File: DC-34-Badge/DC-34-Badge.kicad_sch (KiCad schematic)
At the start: 17 parts, among them U1 ESP32-S3-MINI-1, U2 AP2112K-3.3

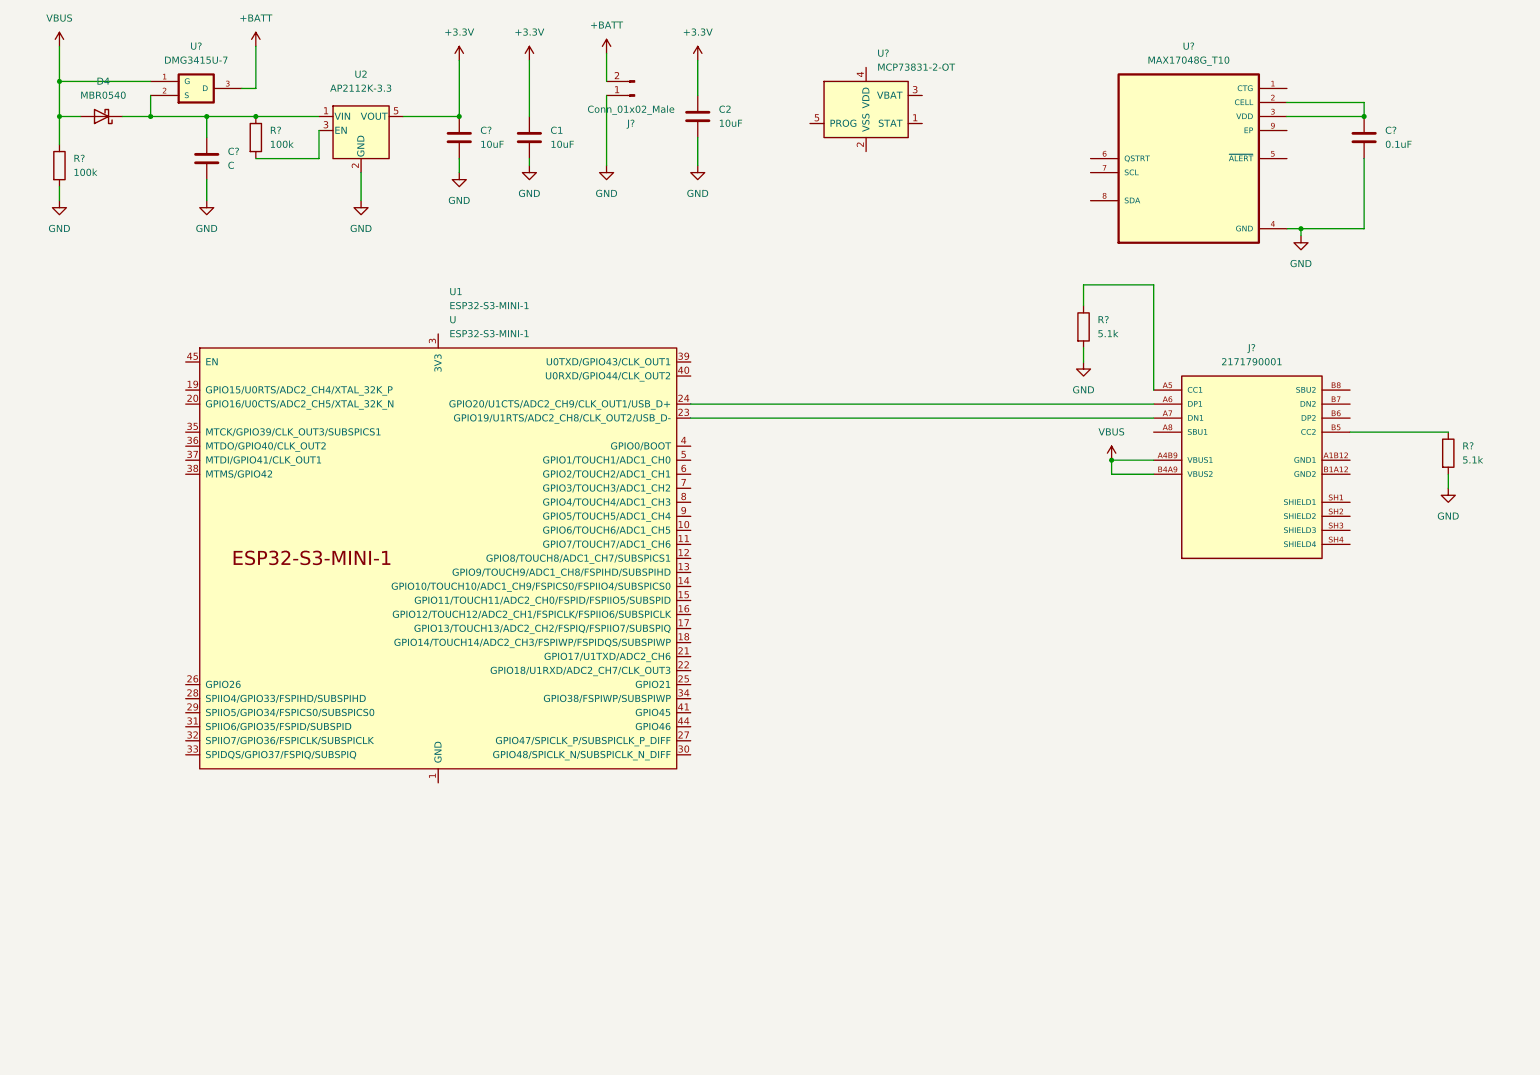
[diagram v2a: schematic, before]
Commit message: Completed Power System
Board design will power up.
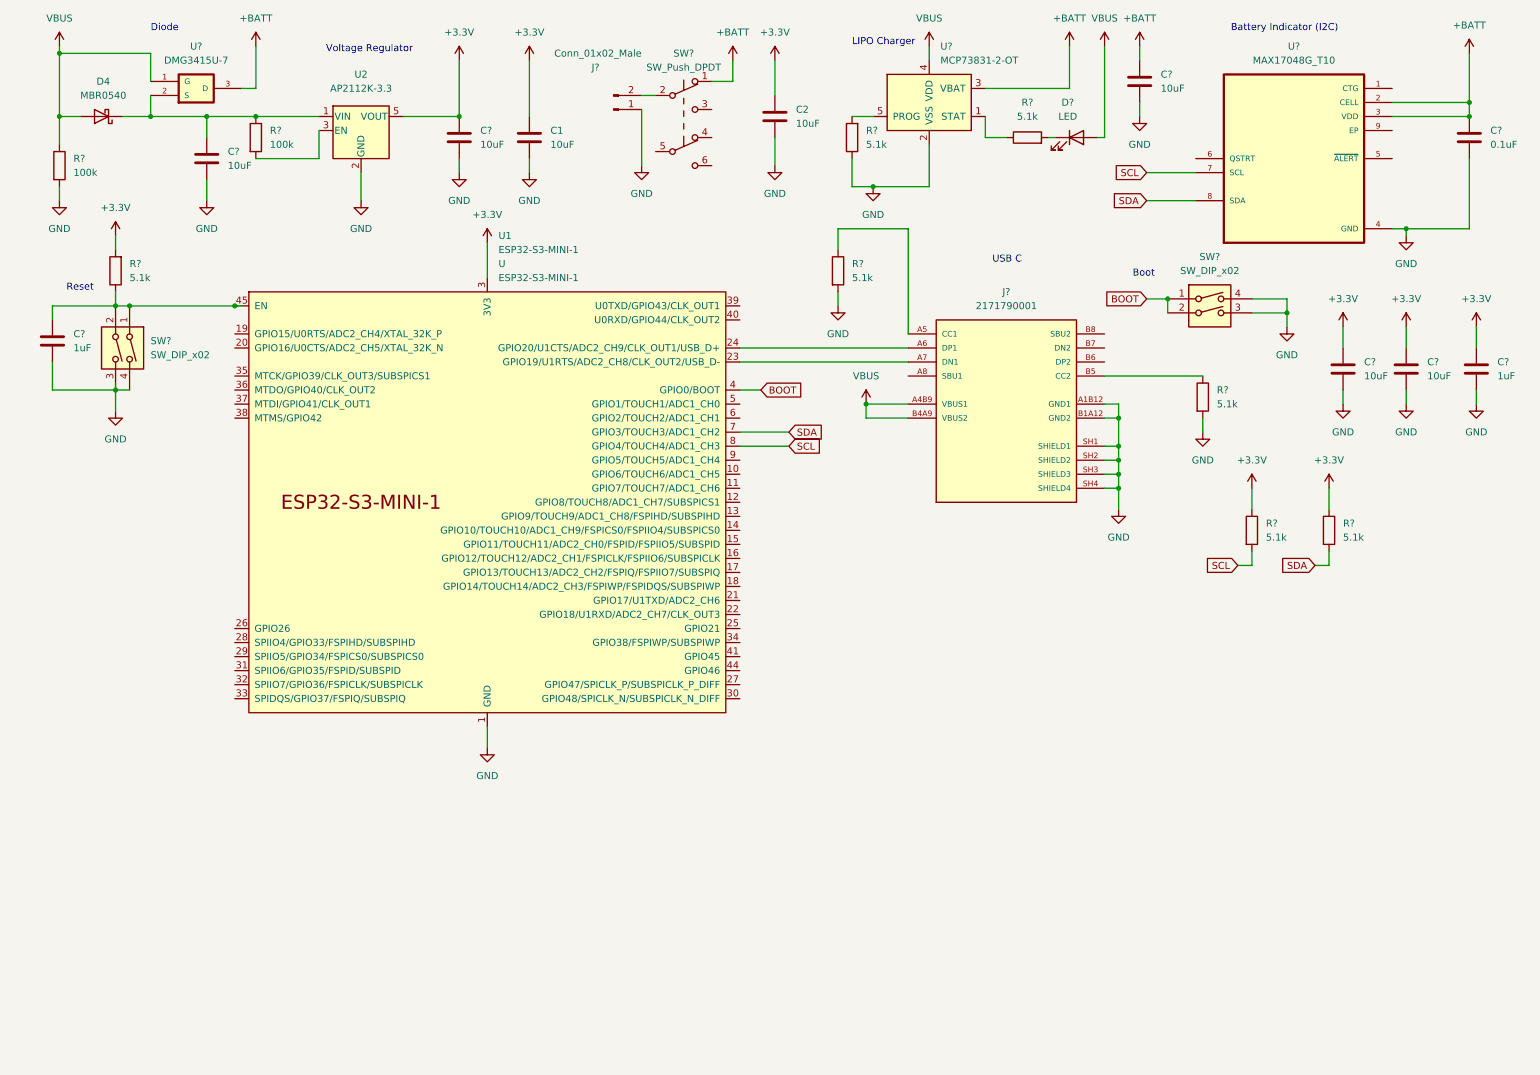
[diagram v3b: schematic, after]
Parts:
- added C? (x2): 1uF, Capacitor_SMD:C_0402_1005Metric, symbol Device:C
- added C? (x3): 10uF, Capacitor_SMD:C_0402_1005Metric, symbol Device:C
- added D?: LED, LED_SMD:LED_0201_0603Metric, symbol Device:LED
- added R? (x5): 5.1k, Resistor_SMD:R_0402_1005Metric, symbol Device:R
- added SW? (x2): SW_DIP_x02, Button_Switch_THT:SW_PUSH_6mm, symbol Switch:SW_DIP_x02
- added SW?: SW_Push_DPDT, Button_Switch_THT:SW_CuK_JS202011CQN_DPDT_Straight, symbol Switch:SW_Push_DPDT
- C?: value C -> 10uF
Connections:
- net +3.3V: now also U1.3 (3V3), C?.1, C?.1, C?.1, R?.1, R?.1, R?.2
- net +BATT: now also C?.1, U?.2 (CELL), U?.3 (VBAT), U?.3 (VDD), C?.1, SW?.1 (A); no longer J?.2 (Pin_2)
- net GND: now also J?.A1B12 (GND1), J?.B1A12 (GND2), J?.SH1 (SHIELD1), J?.SH2 (SHIELD2), J?.SH3 (SHIELD3), J?.SH4 (SHIELD4), U1.1 (GND), U1.2 (GND), U1.42 (GND), U1.43 (GND), U1.46 (GND), U1.47 (GND), U1.48 (GND), U1.49 (GND), U1.50 (GND), U1.51 (GND), U1.52 (GND), U1.53 (GND), U1.54 (GND), U1.55 (GND), U1.56 (GND), U1.57 (GND), U1.58 (GND), U1.59 (GND), U1.60 (GND), U1.61 (GND), U1.62 (GND), U1.63 (GND), U1.64 (GND), U1.65 (GND), U?.2 (VSS), C?.2, C?.2, C?.2, C?.2, C?.2, R?.1, SW?.3, SW?.3, SW?.4, SW?.4
- net VBUS: now also U?.4 (VDD), D?.2 (A)
- net BOOT: now reaches U1.4 (GPIO0/BOOT)
- net BOOT: now also SW?.1, SW?.2
- net at U1.45 (EN): now also C?.1, R?.1, SW?.1, SW?.2
- net SDA: now reaches U1.7 (GPIO3/TOUCH3/ADC1_CH2)
- net SDA: now also U?.8 (SDA), R?.2
- net SCL: now reaches U1.8 (GPIO4/TOUCH4/ADC1_CH3)
- net SCL: now also U?.7 (SCL), R?.2
- net at U?.1 (STAT): now also R?.1
- net at U?.5 (PROG): now also R?.2
- new net: D?.1 (K), R?.2
- new net: J?.2 (Pin_2), SW?.2 (B)
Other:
- note added: "Battery Indicator (I2C)"
- note added: "Boot"
- note added: "Diode"
- note added: "LIPO Charger"
- note added: "Reset"
- note added: "USB C"
- note added: "Voltage Regulator"
- moved on the sheet: C2, C?, J?, R?, U1, U?

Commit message: Base Design Complete
Full duplication of adafruit design.
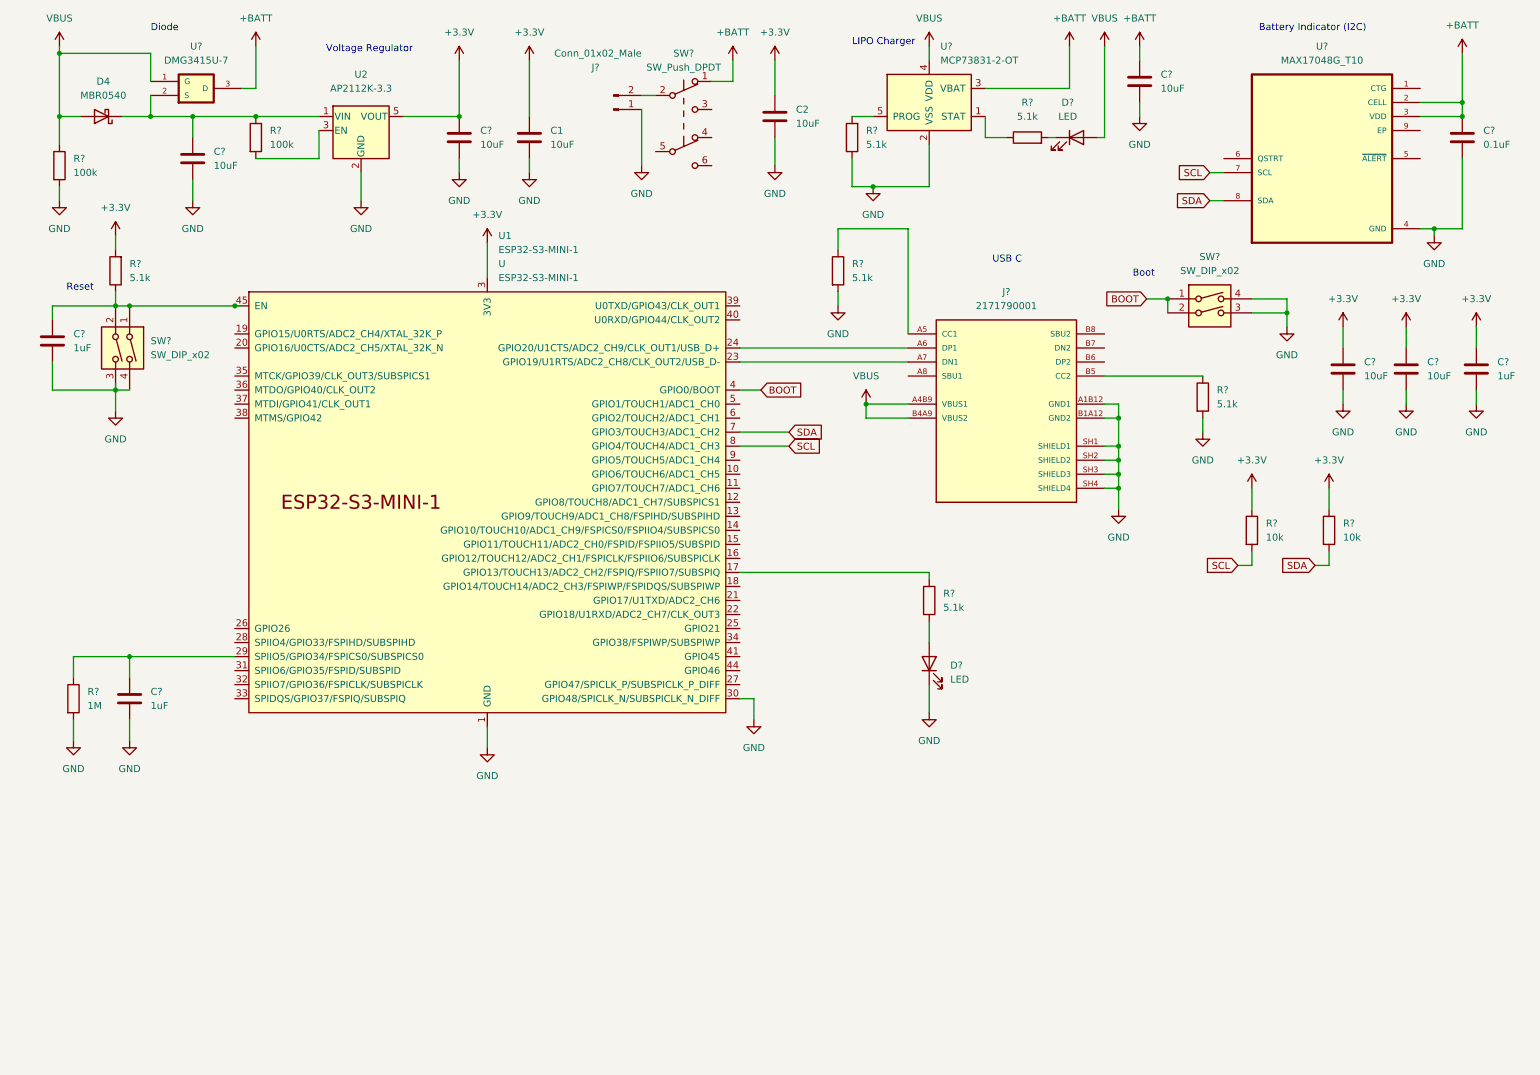
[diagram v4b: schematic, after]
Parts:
- added C?: 1uF, Capacitor_SMD:C_0402_1005Metric, symbol Device:C
- added D?: LED, LED_SMD:LED_0201_0603Metric, symbol Device:LED
- added R?: 1M, Resistor_SMD:R_0402_1005Metric, symbol Device:R
- added R?: 5.1k, Resistor_SMD:R_0402_1005Metric, symbol Device:R
- R? (x2): value 5.1k -> 10k
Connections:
- net GND: now also U1.30 (GPIO48/SPICLK_N/SUBSPICLK_N_DIFF), C?.2, D?.1 (K), R?.2
- net at U1.17 (GPIO13/TOUCH13/ADC2_CH2/FSPIQ/FSPIIO7/SUBSPIQ): now also R?.1
- net at U1.29 (SPIIO5/GPIO34/FSPICS0/SUBSPICS0): now also C?.1, R?.1
- new net: D?.2 (A), R?.2
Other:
- moved on the sheet: C?, U?

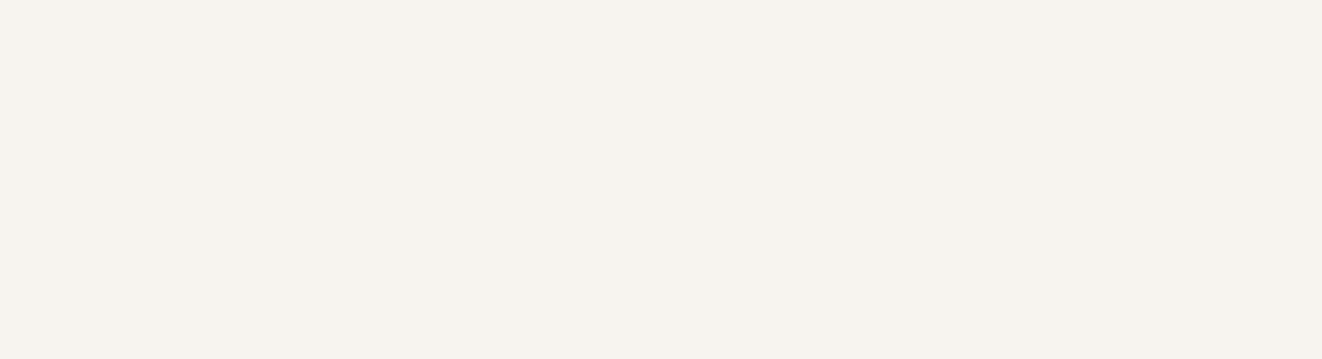
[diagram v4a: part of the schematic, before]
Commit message: Added ZIF Connector
Added ZIF connector symbol and footprint.
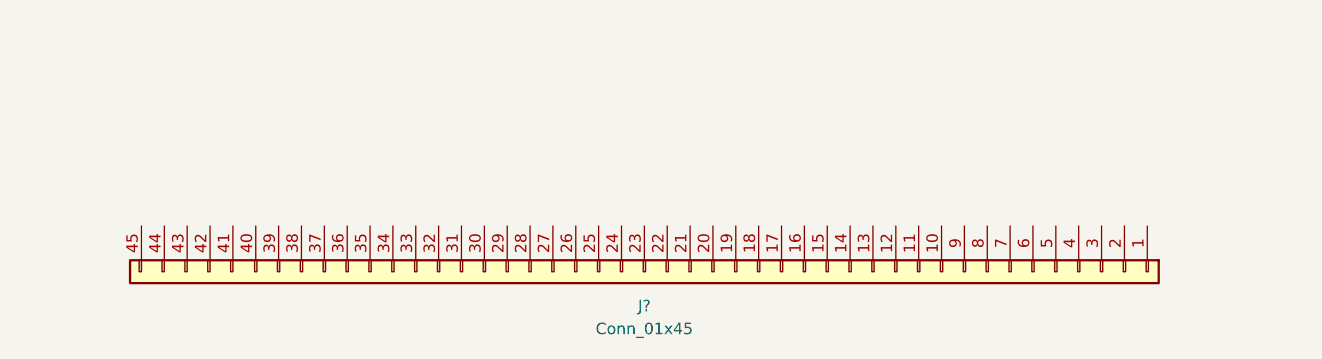
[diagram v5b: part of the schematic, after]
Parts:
- added J?: Conn_01x45, CF4245FH0R0:ZIF_45_0.5mm, symbol ZIF:Conn_01x45
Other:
- company: (none) -> Cyber Professionals Enthusiast Club
- title: (none) -> CPEC DEFCON 34 Badge
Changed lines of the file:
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@@
 (kicad_sch (version 20211123) (generator eeschema)
   (paper "A4")
+  (title_block
+    (title "CPEC DEFCON 34 Badge")
+    (date "3/27/2026")
+    (rev "0.1")
+    (company "Cyber Professionals Enthusiast Club")
+  )
   (junction (at 30.48 66.04) (diameter 0) (color 0 0 0 0)
   )
@@
     )
     (pin "1")
+  )
+  (symbol (lib_id "ZIF:Conn_01x45") (at 93.98 182.88 270) (unit 1)
+    (in_bom yes) (on_board yes) (fields_autoplaced)
+    (property "Reference" "J?" (id 0) (at 86.36 186.69 90))
+    (property "Value" "Conn_01x45" (id 1) (at 86.36 189.23 90))
+    (property "Footprint" "CF4245FH0R0:ZIF_45_0.5mm" (id 2) (at 93.98 182.88 0)
+      (effects (font (size 1.27 1.27)) hide)
+    )
+    (property "Datasheet" "~" (id 3) (at 93.98 182.88 0)
+      (effects (font (size 1.27 1.27)) hide)
+    )
+    (pin "1")
+    (pin "10")
+    (pin "11")
+    (pin "12")
+    (pin "13")
+    (pin "14")
+    (pin "15")
+    (pin "16")
+    (pin "17")
+    (pin "18")
+    (pin "19")
+    (pin "2")
+    (pin "20")
+    (pin "21")
+    (pin "22")
+    (pin "23")
+    (pin "24")
+    (pin "25")
+    (pin "26")
+    (pin "27")
+    (pin "28")
+    (pin "29")
+    (pin "3")
+    (pin "30")
+    (pin "31")
+    (pin "32")
+    (pin "33")
+    (pin "34")
+    (pin "35")
+    (pin "36")
+    (pin "37")
+    (pin "38")
+    (pin "39")
+    (pin "4")
+    (pin "40")
+    (pin "41")
+    (pin "42")
+    (pin "43")
+    (pin "44")
+    (pin "45")
+    (pin "5")
+    (pin "6")
+    (pin "7")
+    (pin "8")
+    (pin "9")
   )
   (symbol (lib_id "power:+3.3V") (at 97.79 54.61 0) (unit 1)
@@
       (reference "D?") (unit 1) (value "LED") (footprint "LED_SMD:LED_0201_0603Metric")
     )
+    (path "/2e34f8c5-d3a8-4e3d-b955-e031e2e6e831"
+      (reference "J?") (unit 1) (value "Conn_01x45") (footprint "CF4245FH0R0:ZIF_45_0.5mm")
+    )
     (path "/67d08764-13cf-4ed9-a103-755c6728deaf"
